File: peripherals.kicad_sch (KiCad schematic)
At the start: 12 parts, among them J3 Conn_01x07_Socket, J4 MSD-4-A

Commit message: Layout completed
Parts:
- removed J3: Conn_01x07_Socket, Connector_JST:JST_XH_S7B-XH-A_1x07_P2.50mm_Horizontal, symbol Connector:Conn_01x07_Socket
- added J5: Conn_01x07_Socket, Connector_JST:JST_PH_S7B-PH-K_1x07_P2.00mm_Horizontal, symbol Connector:Conn_01x07_Socket
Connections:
- net +3.3V: now also J5.2 (Pin_2)
- net GND: now also J5.1 (Pin_1)
- net OLED_CS: now also J5.5 (Pin_5)
- net OLED_DC: now also J5.6 (Pin_6)
- net OLED_RST: now also J5.7 (Pin_7)
- net OLED/SD_MOSI: now also J5.4 (Pin_4)
- net OLED/SD_SCK: now also J5.3 (Pin_3)
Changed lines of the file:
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@@
-	)
-	(symbol
-		(lib_id "Connector:Conn_01x07_Socket")
-		(at 151.13 142.24 0)
-		(unit 1)
-		(exclude_from_sim no)
-		(in_bom yes)
-		(on_board yes)
-		(dnp no)
-		(fields_autoplaced yes)
-		(property "Reference" "J3"
-			(at 156.21 142.24 90)
-			(effects
-				(font
-					(size 1.27 1.27)
-				)
-			)
-		)
-		(property "Value" "Conn_01x07_Socket"
-			(at 153.67 142.24 90)
-			(effects
-				(font
-					(size 1.27 1.27)
-				)
-			)
-		)
-		(property "Footprint" "Connector_JST:JST_XH_S7B-XH-A_1x07_P2.50mm_Horizontal"
-			(at 151.13 142.24 0)
-			(effects
-				(font
-					(size 1.27 1.27)
-				)
-				(hide yes)
-			)
-		)
-		(property "Datasheet" "~"
-			(at 151.13 142.24 0)
-			(effects
-				(font
-					(size 1.27 1.27)
-				)
-				(hide yes)
-			)
-		)
-		(property "Description" "Generic connector, single row, 01x07, script generated"
-			(at 151.13 142.24 0)
-			(effects
-				(font
-					(size 1.27 1.27)
-				)
-				(hide yes)
-			)
-		)
-		(property "Distributor Link" "https://www.digikey.com/en/products/detail/jst-sales-america-inc/S7B-XH-A/1651038"
-			(at 151.13 142.24 90)
-			(effects
-				(font
-					(size 1.27 1.27)
-				)
-				(hide yes)
-			)
-		)
-		(property "MPN" "S7B-XH-A"
-			(at 151.13 142.24 90)
-			(effects
-				(font
-					(size 1.27 1.27)
-				)
-				(hide yes)
-			)
-		)
-		(property "Manufacturer" "JST Sales America Inc."
-			(at 151.13 142.24 90)
-			(effects
-				(font
-					(size 1.27 1.27)
-				)
-				(hide yes)
-			)
-		)
-		(pin "1"
-		)
-		(pin "3"
-		)
-		(pin "5"
-		)
-		(pin "7"
-		)
-		(pin "2"
-		)
-		(pin "4"
-		)
-		(pin "6"
-		)
-		(instances
-			(project "ESP32_Tracker"
-				(path "/92195c42-0bc4-473e-a890-6f85786d3c69/397d7a99-8f38-42c5-a73f-5d1ccdc57b5a"
-					(reference "J3")
-					(unit 1)
-				)
-			)
-		)
 	)
 	(symbol
@@
 					(unit 1)
 				)
+			)
+		)
+	)
+	(symbol
+		(lib_id "Connector:Conn_01x07_Socket")
+		(at 151.13 142.24 0)
+		(unit 1)
+		(exclude_from_sim no)
+		(in_bom yes)
+		(on_board yes)
+		(dnp no)
+		(fields_autoplaced yes)
+		(property "Reference" "J5"
+			(at 156.21 142.24 90)
+			(effects
+				(font
+					(size 1.27 1.27)
+				)
+			)
+		)
+		(property "Value" "Conn_01x07_Socket"
+			(at 153.67 142.24 90)
+			(effects
+				(font
+					(size 1.27 1.27)
+				)
+			)
+		)
+		(property "Footprint" "Connector_JST:JST_PH_S7B-PH-K_1x07_P2.00mm_Horizontal"
+			(at 151.13 142.24 0)
+			(effects
+				(font
+					(size 1.27 1.27)
+				)
+				(hide yes)
+			)
+		)
+		(property "Datasheet" "~"
+			(at 151.13 142.24 0)
+			(effects
+				(font
+					(size 1.27 1.27)
+				)
+				(hide yes)
+			)
+		)
+		(property "Description" "Generic connector, single row, 01x07, script generated"
+			(at 151.13 142.24 0)
+			(effects
+				(font
+					(size 1.27 1.27)
+				)
+				(hide yes)
+			)
+		)
+		(property "Distributor Link" "https://www.digikey.com/en/products/detail/jst-sales-america-inc/S7B-PH-K-S/926631"
+			(at 151.13 142.24 90)
+			(effects
+				(font
+					(size 1.27 1.27)
+				)
+				(hide yes)
+			)
+		)
+		(property "MPN" "S7B-PH-K-S"
+			(at 151.13 142.24 90)
+			(effects
+				(font
+					(size 1.27 1.27)
+				)
+				(hide yes)
+			)
+		)
+		(property "Manufacturer" "JST Sales America Inc."
+			(at 151.13 142.24 90)
+			(effects
+				(font
+					(size 1.27 1.27)
+				)
+				(hide yes)
+			)
+		)
+		(pin "1"
+		)
+		(pin "3"
+		)
+		(pin "5"
+		)
+		(pin "7"
+		)
+		(pin "2"
+		)
+		(pin "4"
+		)
+		(pin "6"
+		)
+		(instances
+			(project "ESP32_Tracker"
+				(path "/92195c42-0bc4-473e-a890-6f85786d3c69/397d7a99-8f38-42c5-a73f-5d1ccdc57b5a"
+					(reference "J5")
+					(unit 1)
+				)

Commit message: modified and labeled layout
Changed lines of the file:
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@@
 	(text "2.42\" OLED display"
 		(exclude_from_sim no)
-		(at 120.396 109.982 0)
+		(at 118.872 112.014 0)
 		(effects
 			(font

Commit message: modified BOM
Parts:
- C19, C22: Distributor Link https://www.lcsc.com/product-detail/C95841.html -> https://www.digikey.com/en/products/detail/samsung-electro-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
- C20, C21: Distributor Link https://www.lcsc.com/product-detail/C519980.html -> https://www.digikey.com/en/products/detail/samsung-electro-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; MPN CC0805KRX7R7BB104 -> CL21B104KBCNNNC; Manufacturer YAGEO -> Samsung Electro-Mechanics
- R18, R19, R20, R21, R22, R23: Distributor Link https://www.lcsc.com/product-detail/C17414.html -> https://www.digikey.com/en/products/detail/yageo/RC0805JR-0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; MPN 0805W8F1002T5E -> RC0805JR-0710KL; Manufacturer UNI-ROYAL -> YAGEO
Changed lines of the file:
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@@
 			)
 		)
-		(property "Datasheet" "https://www.lcsc.com/datasheet/C95841.pdf"
+		(property "Datasheet" ""
 			(at 113.03 128.27 0)
 			(effects
@@
 			)
 		)
-		(property "Distributor Link" "https://www.lcsc.com/product-detail/C95841.html"
+		(property "Distributor Link" "https://www.digikey.com/en/products/detail/samsung-electro-mechanics/CL21B106KOQNNNE/3888530"
+			(at 113.03 128.27 0)
+			(effects
+				(font
+					(size 1.27 1.27)
+				)
+				(hide yes)
+			)
+		)
+		(property "DIGIKEY" ""
 			(at 113.03 128.27 0)
 			(effects
@@
 			)
 		)
-		(property "Datasheet" "https://www.lcsc.com/datasheet/C519980.pdf"
+		(property "Datasheet" ""
 			(at 147.32 40.64 0)
 			(effects
@@
 			)
 		)
-		(property "MPN" "CC0805KRX7R7BB104"
+		(property "MPN" "CL21B104KBCNNNC"
 			(at 147.32 40.64 0)
 			(effects
@@
 			)
 		)
-		(property "Manufacturer" "YAGEO"
+		(property "Manufacturer" "Samsung Electro-Mechanics"
 			(at 147.32 40.64 0)
 			(effects
@@
 			)
 		)
-		(property "Distributor Link" "https://www.lcsc.com/product-detail/C519980.html"
+		(property "Distributor Link" "https://www.digikey.com/en/products/detail/samsung-electro-mechanics/CL21B104KBCNNNC/3886661"
+			(at 147.32 40.64 0)
+			(effects
+				(font
+					(size 1.27 1.27)
+				)
+				(hide yes)
+			)
+		)
+		(property "DIGIKEY" ""
 			(at 147.32 40.64 0)
 			(effects
@@
 			)
 		)
-		(property "Datasheet" "https://www.lcsc.com/datasheet/C519980.pdf"
+		(property "Datasheet" ""
 			(at 123.19 128.27 0)
 			(effects
@@
 			)
 		)
-		(property "MPN" "CC0805KRX7R7BB104"
+		(property "MPN" "CL21B104KBCNNNC"
 			(at 123.19 128.27 0)
 			(effects
@@
 			)
 		)
-		(property "Manufacturer" "YAGEO"
+		(property "Manufacturer" "Samsung Electro-Mechanics"
 			(at 123.19 128.27 0)
 			(effects
@@
 			)
 		)
-		(property "Distributor Link" "https://www.lcsc.com/product-detail/C519980.html"
+		(property "Distributor Link" "https://www.digikey.com/en/products/detail/samsung-electro-mechanics/CL21B104KBCNNNC/3886661"
+			(at 123.19 128.27 0)
+			(effects
+				(font
+					(size 1.27 1.27)
+				)
+				(hide yes)
+			)
+		)
+		(property "DIGIKEY" ""
 			(at 123.19 128.27 0)
 			(effects
@@
 			)
 		)
-		(property "Datasheet" "https://www.lcsc.com/datasheet/C17414.pdf"
+		(property "Datasheet" ""
 			(at 129.54 129.54 0)
 			(effects
@@
 			)
 		)
-		(property "MPN" "0805W8F1002T5E"
+		(property "MPN" "RC0805JR-0710KL"
 			(at 129.54 129.54 0)
 			(effects
@@
 			)
 		)
-		(property "Manufacturer" "UNI-ROYAL"
+		(property "Manufacturer" "YAGEO"
 			(at 129.54 129.54 0)
 			(effects
@@
 			)
 		)
-		(property "Distributor Link" "https://www.lcsc.com/product-detail/C17414.html"
+		(property "Distributor Link" "https://www.digikey.com/en/products/detail/yageo/RC0805JR-0710KL/728241"
+			(at 129.54 129.54 0)
+			(effects
+				(font
+					(size 1.27 1.27)
+				)
+				(hide yes)
+			)
+		)
+		(property "DIGIKEY" ""
 			(at 129.54 129.54 0)
 			(effects
@@
 			)
 		)
-		(property "Datasheet" "https://www.lcsc.com/datasheet/C17414.pdf"
+		(property "Datasheet" ""
 			(at 111.76 41.91 0)
 			(effects
@@
 			)
 		)
-		(property "MPN" "0805W8F1002T5E"
+		(property "MPN" "RC0805JR-0710KL"
 			(at 111.76 41.91 90)
 			(effects
@@
 			)
 		)
-		(property "Manufacturer" "UNI-ROYAL"
+		(property "Manufacturer" "YAGEO"
 			(at 111.76 41.91 90)
 			(effects
@@
 			)
 		)
-		(property "Distributor Link" "https://www.lcsc.com/product-detail/C17414.html"
+		(property "Distributor Link" "https://www.digikey.com/en/products/detail/yageo/RC0805JR-0710KL/728241"
+			(at 111.76 41.91 90)
+			(effects
+				(font
+					(size 1.27 1.27)
+				)
+				(hide yes)
+			)
+		)
+		(property "DIGIKEY" ""
 			(at 111.76 41.91 90)
 			(effects
@@
 			)
 		)
-		(property "Datasheet" "https://www.lcsc.com/datasheet/C17414.pdf"
+		(property "Datasheet" ""
 			(at 137.16 41.91 0)
 			(effects
@@
 			)
 		)
-		(property "MPN" "0805W8F1002T5E"
+		(property "MPN" "RC0805JR-0710KL"
 			(at 137.16 41.91 90)
 			(effects
@@
 			)
 		)
-		(property "Manufacturer" "UNI-ROYAL"
+		(property "Manufacturer" "YAGEO"
 			(at 137.16 41.91 90)
 			(effects
@@
 			)
 		)
-		(property "Distributor Link" "https://www.lcsc.com/product-detail/C17414.html"
+		(property "Distributor Link" "https://www.digikey.com/en/products/detail/yageo/RC0805JR-0710KL/728241"
+			(at 137.16 41.91 90)
+			(effects
+				(font
+					(size 1.27 1.27)
+				)
+				(hide yes)
+			)
+		)
+		(property "DIGIKEY" ""
 			(at 137.16 41.91 90)
 			(effects
@@
 			)
 		)
-		(property "Datasheet" "https://www.lcsc.com/datasheet/C17414.pdf"
+		(property "Datasheet" ""
 			(at 118.11 41.91 0)
 			(effects
@@
 			)
 		)
-		(property "MPN" "0805W8F1002T5E"
+		(property "MPN" "RC0805JR-0710KL"
 			(at 118.11 41.91 90)
 			(effects
@@
 			)
 		)
-		(property "Manufacturer" "UNI-ROYAL"
+		(property "Manufacturer" "YAGEO"
 			(at 118.11 41.91 90)
 			(effects
@@
 			)
 		)
-		(property "Distributor Link" "https://www.lcsc.com/product-detail/C17414.html"
+		(property "Distributor Link" "https://www.digikey.com/en/products/detail/yageo/RC0805JR-0710KL/728241"
+			(at 118.11 41.91 90)
+			(effects
+				(font
+					(size 1.27 1.27)
+				)
+				(hide yes)
+			)
+		)
+		(property "DIGIKEY" ""
 			(at 118.11 41.91 90)
 			(effects
@@
 			)
 		)
+		(property "DIGIKEY" ""
+			(at 181.61 69.85 0)
+			(effects
+				(font
+					(size 1.27 1.27)
+				)
+				(hide yes)
+			)
+		)
 		(pin "6"
 		)
@@
 			)
 		)
-		(property "Datasheet" "https://www.lcsc.com/datasheet/C17414.pdf"
+		(property "Datasheet" ""
 			(at 130.81 41.91 0)
 			(effects
@@
 			)
 		)
-		(property "MPN" "0805W8F1002T5E"
+		(property "MPN" "RC0805JR-0710KL"
 			(at 130.81 41.91 90)
 			(effects
@@
 			)
 		)
-		(property "Manufacturer" "UNI-ROYAL"
+		(property "Manufacturer" "YAGEO"
 			(at 130.81 41.91 90)
 			(effects
@@
 			)
 		)
-		(property "Distributor Link" "https://www.lcsc.com/product-detail/C17414.html"
+		(property "Distributor Link" "https://www.digikey.com/en/products/detail/yageo/RC0805JR-0710KL/728241"
+			(at 130.81 41.91 90)
+			(effects
+				(font
+					(size 1.27 1.27)
+				)
+				(hide yes)
+			)
+		)
+		(property "DIGIKEY" ""
 			(at 130.81 41.91 90)
 			(effects
@@
 			)
 		)
-		(property "Datasheet" "https://www.lcsc.com/datasheet/C95841.pdf"
+		(property "Datasheet" ""
 			(at 158.75 40.64 0)
 			(effects
@@
 			)
 		)
-		(property "Distributor Link" "https://www.lcsc.com/product-detail/C95841.html"
+		(property "Distributor Link" "https://www.digikey.com/en/products/detail/samsung-electro-mechanics/CL21B106KOQNNNE/3888530"
+			(at 158.75 40.64 0)
+			(effects
+				(font
+					(size 1.27 1.27)
+				)
+				(hide yes)
+			)
+		)
+		(property "DIGIKEY" ""
 			(at 158.75 40.64 0)
 			(effects
@@
 			)
 		)
-		(property "Datasheet" "https://www.lcsc.com/datasheet/C17414.pdf"
+		(property "Datasheet" ""
 			(at 124.46 41.91 0)
 			(effects
@@
 			)
 		)
-		(property "MPN" "0805W8F1002T5E"
+		(property "MPN" "RC0805JR-0710KL"
 			(at 124.46 41.91 90)
 			(effects
@@
 			)
 		)
-		(property "Manufacturer" "UNI-ROYAL"
+		(property "Manufacturer" "YAGEO"
 			(at 124.46 41.91 90)
 			(effects
@@
 			)
 		)
-		(property "Distributor Link" "https://www.lcsc.com/product-detail/C17414.html"
+		(property "Distributor Link" "https://www.digikey.com/en/products/detail/yageo/RC0805JR-0710KL/728241"
+			(at 124.46 41.91 90)
+			(effects
+				(font
+					(size 1.27 1.27)
+				)
+				(hide yes)
+			)
+		)
+		(property "DIGIKEY" ""
 			(at 124.46 41.91 90)
 			(effects
@@
 			(at 151.13 142.24 90)
 			(effects
+				(font
+					(size 1.27 1.27)
+				)
+				(hide yes)
+			)
+		)
+		(property "DIGIKEY" ""
+			(at 151.13 142.24 90)
+			(effects

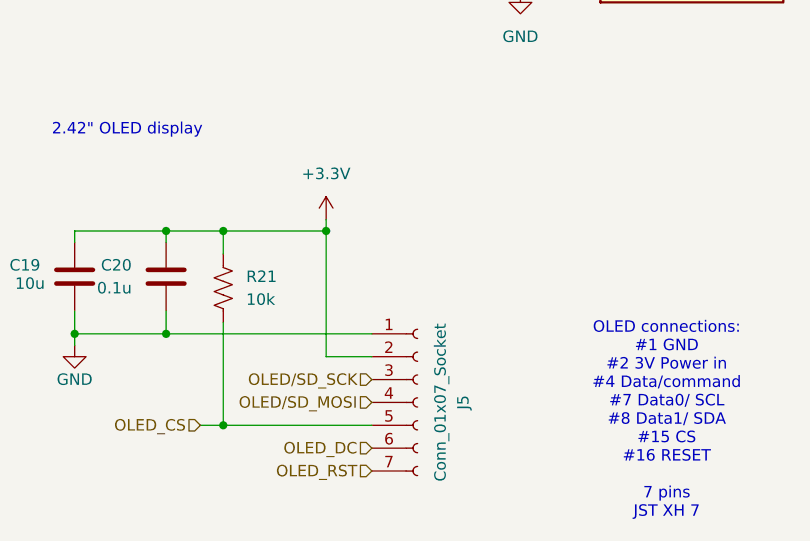
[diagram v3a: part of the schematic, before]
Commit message: changed to 8 pin connector
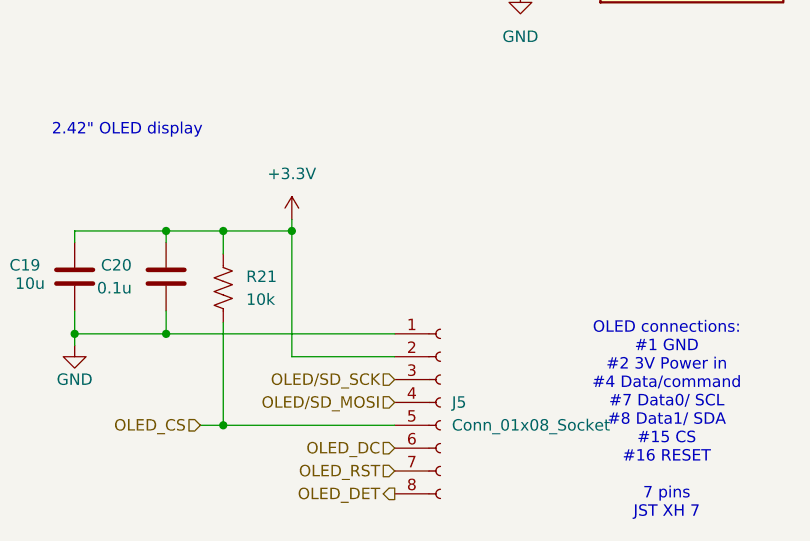
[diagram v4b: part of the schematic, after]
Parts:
- removed J5: Conn_01x07_Socket, Connector_JST:JST_PH_S7B-PH-K_1x07_P2.00mm_Horizontal, symbol Connector:Conn_01x07_Socket
- added J5: Conn_01x08_Socket, Connector_JST:JST_PH_S8B-PH-K_1x08_P2.00mm_Horizontal, symbol Connector:Conn_01x08_Socket
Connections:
- net +3.3V: now also J5.2 (Pin_2)
- net GND: now also J5.1 (Pin_1)
- net OLED_CS: now also J5.5 (Pin_5)
- net OLED_DC: now also J5.6 (Pin_6)
- net OLED_RST: now also J5.7 (Pin_7)
- net OLED/SD_MOSI: now also J5.4 (Pin_4)
- net OLED/SD_SCK: now also J5.3 (Pin_3)
- new net OLED_DET: J5.8 (Pin_8)
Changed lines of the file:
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@@
-	)
-	(junction
-		(at 140.97 123.19)
-		(diameter 0)
-		(color 0 0 0 0)
 	)
 	(junction
@@
 	)
 	(junction
+		(at 137.16 123.19)
+		(diameter 0)
+		(color 0 0 0 0)
+	)
+	(junction
 		(at 123.19 134.62)
 		(diameter 0)
@@
 	(wire
 		(pts
-			(xy 146.05 137.16) (xy 140.97 137.16)
+			(xy 148.59 137.16) (xy 137.16 137.16)
 		)
 		(stroke
@@
 	(wire
 		(pts
-			(xy 140.97 121.92) (xy 140.97 123.19)
+			(xy 137.16 121.92) (xy 137.16 123.19)
 		)
 		(stroke
@@
 	(wire
 		(pts
-			(xy 140.97 123.19) (xy 140.97 137.16)
+			(xy 137.16 123.19) (xy 137.16 137.16)
 		)
 		(stroke
@@
 	(wire
 		(pts
-			(xy 129.54 144.78) (xy 146.05 144.78)
+			(xy 129.54 144.78) (xy 148.59 144.78)
 		)
 		(stroke
@@
 	(wire
 		(pts
-			(xy 123.19 134.62) (xy 146.05 134.62)
+			(xy 123.19 134.62) (xy 148.59 134.62)
 		)
 		(stroke
@@
 	(wire
 		(pts
-			(xy 129.54 123.19) (xy 140.97 123.19)
+			(xy 129.54 123.19) (xy 137.16 123.19)
 		)
 		(stroke
@@
 	(hierarchical_label "OLED{slash}SD_MOSI"
 		(shape input)
-		(at 146.05 142.24 180)
+		(at 148.59 142.24 180)
 		(effects
 			(font
@@
 		)
 	)
+	(hierarchical_label "OLED_DET"
+		(shape output)
+		(at 148.59 152.4 180)
+		(effects
+			(font
+				(size 1.27 1.27)
+			)
+			(justify right)
+		)
+	)
 	(hierarchical_label "OLED{slash}SD_SCK"
 		(shape input)
-		(at 146.05 139.7 180)
+		(at 148.59 139.7 180)
 		(effects
 			(font
@@
 	(hierarchical_label "OLED_RST"
 		(shape input)
-		(at 146.05 149.86 180)
+		(at 148.59 149.86 180)
 		(effects
 			(font
@@
 	(hierarchical_label "OLED_DC"
 		(shape input)
-		(at 146.05 147.32 180)
+		(at 148.59 147.32 180)
 		(effects
 			(font
@@
 	(symbol
 		(lib_id "power:+3.3V")
-		(at 140.97 121.92 0)
+		(at 137.16 121.92 0)
 		(unit 1)
 		(exclude_from_sim no)
@@
 		(fields_autoplaced yes)
 		(property "Reference" "#PWR037"
-			(at 140.97 125.73 0)
+			(at 137.16 125.73 0)
 			(effects
 				(font
@@
 		)
 		(property "Value" "+3.3V"
-			(at 140.97 116.84 0)
+			(at 137.16 116.84 0)
 			(effects
 				(font
@@
 		)
 		(property "Footprint" ""
-			(at 140.97 121.92 0)
+			(at 137.16 121.92 0)
 			(effects
 				(font
@@
 		)
 		(property "Datasheet" ""
-			(at 140.97 121.92 0)
+			(at 137.16 121.92 0)
 			(effects
 				(font
@@
 		)
 		(property "Description" "Power symbol creates a global label with name \"+3.3V\""
-			(at 140.97 121.92 0)
+			(at 137.16 121.92 0)
 			(effects
 				(font
@@
 	)
 	(symbol
+		(lib_id "Connector:Conn_01x08_Socket")
+		(at 153.67 142.24 0)
+		(unit 1)
+		(exclude_from_sim no)
+		(in_bom yes)
+		(on_board yes)
+		(dnp no)
+		(fields_autoplaced yes)
+		(property "Reference" "J5"
+			(at 154.94 142.2399 0)
+			(effects
+				(font
+					(size 1.27 1.27)
+				)
+				(justify left)
+			)
+		)
+		(property "Value" "Conn_01x08_Socket"
+			(at 154.94 144.7799 0)
+			(effects
+				(font
+					(size 1.27 1.27)
+				)
+				(justify left)
+			)
+		)
+		(property "Footprint" "Connector_JST:JST_PH_S8B-PH-K_1x08_P2.00mm_Horizontal"
+			(at 153.67 142.24 0)
+			(effects
+				(font
+					(size 1.27 1.27)
+				)
+				(hide yes)
+			)
+		)
+		(property "Datasheet" "~"
+			(at 153.67 142.24 0)
+			(effects
+				(font
+					(size 1.27 1.27)
+				)
+				(hide yes)
+			)
+		)
+		(property "Description" "Generic connector, single row, 01x08, script generated"
+			(at 153.67 142.24 0)
+			(effects
+				(font
+					(size 1.27 1.27)
+				)
+				(hide yes)
+			)
+		)
+		(property "Distributor Link" "https://www.digikey.com/en/products/detail/jst-sales-america-inc/S8B-PH-K-S/926632?s=N4IgTCBcDaIMoA4BCBaACgCRQaRXEAugL5A"
+			(at 153.67 142.24 0)
+			(effects
+				(font
+					(size 1.27 1.27)
+				)
+				(hide yes)
+			)
+		)
+		(property "MPN" "S8B-PH-K-S"
+			(at 153.67 142.24 0)
+			(effects
+				(font
+					(size 1.27 1.27)
+				)
+				(hide yes)
+			)
+		)
+		(property "Manufacturer" "JST Sales America Inc."
+			(at 153.67 142.24 0)
+			(effects
+				(font
+					(size 1.27 1.27)
+				)
+				(hide yes)
+			)
+		)
+		(pin "4"
+		)
+		(pin "3"
+		)
+		(pin "7"
+		)
+		(pin "8"
+		)
+		(pin "1"
+		)
+		(pin "6"
+		)
+		(pin "2"
+		)
+		(pin "5"
+		)
+		(instances
+			(project "ESP32_Tracker"
+				(path "/92195c42-0bc4-473e-a890-6f85786d3c69/397d7a99-8f38-42c5-a73f-5d1ccdc57b5a"
+					(reference "J5")
+					(unit 1)
+				)
+			)
+		)
+	)
+	(symbol
 		(lib_id "Device:R_US")
 		(at 111.76 41.91 0)
@@
 					(unit 1)
 				)
-			)
-		)
-	)
-	(symbol
-		(lib_id "Connector:Conn_01x07_Socket")
-		(at 151.13 142.24 0)
-		(unit 1)
-		(exclude_from_sim no)
-		(in_bom yes)
-		(on_board yes)
-		(dnp no)
-		(fields_autoplaced yes)
-		(property "Reference" "J5"
-			(at 156.21 142.24 90)
-			(effects
-				(font
-					(size 1.27 1.27)
-				)
-			)
-		)
-		(property "Value" "Conn_01x07_Socket"
-			(at 153.67 142.24 90)
-			(effects
-				(font
-					(size 1.27 1.27)
-				)
-			)
-		)
-		(property "Footprint" "Connector_JST:JST_PH_S7B-PH-K_1x07_P2.00mm_Horizontal"
-			(at 151.13 142.24 0)
-			(effects
-				(font
-					(size 1.27 1.27)
-				)
-				(hide yes)
-			)
-		)
-		(property "Datasheet" "~"
-			(at 151.13 142.24 0)
-			(effects
-				(font
-					(size 1.27 1.27)
-				)
-				(hide yes)
-			)
-		)
-		(property "Description" "Generic connector, single row, 01x07, script generated"
-			(at 151.13 142.24 0)
-			(effects
-				(font
-					(size 1.27 1.27)
-				)
-				(hide yes)
-			)
-		)
-		(property "Distributor Link" "https://www.digikey.com/en/products/detail/jst-sales-america-inc/S7B-PH-K-S/926631"
-			(at 151.13 142.24 90)
-			(effects
-				(font
-					(size 1.27 1.27)
-				)
-				(hide yes)
-			)
-		)
-		(property "MPN" "S7B-PH-K-S"
-			(at 151.13 142.24 90)
-			(effects
-				(font
-					(size 1.27 1.27)
-				)
-				(hide yes)
-			)
-		)
-		(property "Manufacturer" "JST Sales America Inc."
-			(at 151.13 142.24 90)
-			(effects
-				(font
-					(size 1.27 1.27)
-				)
-				(hide yes)
-			)
-		)
-		(property "DIGIKEY" ""
-			(at 151.13 142.24 90)
-			(effects
-				(font
-					(size 1.27 1.27)
-				)
-				(hide yes)
-			)
-		)
-		(pin "1"
-		)
-		(pin "3"
-		)
-		(pin "5"
-		)
-		(pin "7"
-		)
-		(pin "2"
-		)
-		(pin "4"
-		)
-		(pin "6"
-		)
-		(instances
-			(project "ESP32_Tracker"
-				(path "/92195c42-0bc4-473e-a890-6f85786d3c69/397d7a99-8f38-42c5-a73f-5d1ccdc57b5a"
-					(reference "J5")
-					(unit 1)
-				)
